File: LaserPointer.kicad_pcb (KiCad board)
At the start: 2 copper layers, 100.3 x 20.3 mm, 10 parts, among them J1 Laser Diode - 5mW 650nm Red, SW1 Mini Soft Touch Push-button S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, U1 MCP1640Bx-xCHY

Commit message: Finished
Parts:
- added H1: MountingHole_2.2mm_M2, MountingHole:MountingHole_2.2mm_M2, F.Cu at (71.1, 62.2)
- added H2: MountingHole_2.2mm_M2, MountingHole:MountingHole_2.2mm_M2, F.Cu at (156.2, 74.9)
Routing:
- net GND: vias 2 -> 4
- added copper zone on B.Cu, net GND
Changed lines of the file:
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@@
 		)
+	)
+	(footprint "MountingHole:MountingHole_2.2mm_M2"
+		(layer "F.Cu")
+		(at 156.21 74.93)
+		(descr "Mounting Hole 2.2mm, M2, no annular, generated by kicad-footprint-generator mountinghole.py")
+		(tags "mountinghole M2")
+		(property "Reference" "H2"
+			(at 0 -3.15 0)
+			(layer "F.SilkS")
+			(hide yes)
+			(effects
+				(font
+					(size 1 1)
+					(thickness 0.15)
+				)
+			)
+		)
+		(property "Value" "MountingHole_2.2mm_M2"
+			(at 0 3.15 0)
+			(layer "F.Fab")
+			(hide yes)
+			(effects
+				(font
+					(size 1 1)
+					(thickness 0.15)
+				)
+			)
+		)
+		(property "Datasheet" ""
+			(at 0 0 0)
+			(layer "F.Fab")
+			(hide yes)
+			(effects
+				(font
+					(size 1.27 1.27)
+				)
+			)
+		)
+		(property "Description" ""
+			(at 0 0 0)
+			(layer "F.Fab")
+			(hide yes)
+			(effects
+				(font
+					(size 1.27 1.27)
+				)
+			)
+		)
+		(property "KiLib_Generator" "mounting_hardware/mounting_hole"
+			(at 0 0 0)
+			(layer "F.SilkS")
+			(hide yes)
+			(effects
+				(font
+					(size 1 1)
+					(thickness 0.15)
+				)
+			)
+		)
+		(attr exclude_from_pos_files exclude_from_bom)
+		(duplicate_pad_numbers_are_jumpers no)
+		(fp_circle
+			(center 0 0)
+			(end 2.2 0)
+			(stroke
+				(width 0.15)
+				(type solid)
+			)
+			(fill no)
+			(layer "Cmts.User")
+		)
+		(fp_circle
+			(center 0 0)
+			(end 2.45 0)
+			(stroke
+				(width 0.05)
+				(type solid)
+			)
+			(fill no)
+			(layer "F.CrtYd")
+		)
+		(fp_text user "H2"
+			(at 0 0 0)
+			(layer "F.Fab")
+			(effects
+				(font
+					(size 1 1)
+					(thickness 0.15)
+				)
+			)
+		)
+		(pad "" np_thru_hole circle
+			(at 0 0)
+			(size 2.2 2.2)
+			(drill 2.2)
+			(layers "*.Cu" "*.Mask")
+		)
+		(embedded_fonts no)
 	)
 	(footprint "Capacitor_SMD:C_0805_2012Metric"
@@
 		(embedded_fonts no)
 	)
+	(footprint "MountingHole:MountingHole_2.2mm_M2"
+		(layer "F.Cu")
+		(at 71.12 62.23)
+		(descr "Mounting Hole 2.2mm, M2, no annular, generated by kicad-footprint-generator mountinghole.py")
+		(tags "mountinghole M2")
+		(property "Reference" "H1"
+			(at 0 -3.15 0)
+			(layer "F.SilkS")
+			(hide yes)
+			(effects
+				(font
+					(size 1 1)
+					(thickness 0.15)
+				)
+			)
+		)
+		(property "Value" "MountingHole_2.2mm_M2"
+			(at 0 3.15 0)
+			(layer "F.Fab")
+			(hide yes)
+			(effects
+				(font
+					(size 1 1)
+					(thickness 0.15)
+				)
+			)
+		)
+		(property "Datasheet" ""
+			(at 0 0 0)
+			(layer "F.Fab")
+			(hide yes)
+			(effects
+				(font
+					(size 1.27 1.27)
+				)
+			)
+		)
+		(property "Description" ""
+			(at 0 0 0)
+			(layer "F.Fab")
+			(hide yes)
+			(effects
+				(font
+					(size 1.27 1.27)
+				)
+			)
+		)
+		(property "KiLib_Generator" "mounting_hardware/mounting_hole"
+			(at 0 0 0)
+			(layer "F.SilkS")
+			(hide yes)
+			(effects
+				(font
+					(size 1 1)
+					(thickness 0.15)
+				)
+			)
+		)
+		(attr exclude_from_pos_files exclude_from_bom)
+		(duplicate_pad_numbers_are_jumpers no)
+		(fp_circle
+			(center 0 0)
+			(end 2.2 0)
+			(stroke
+				(width 0.15)
+				(type solid)
+			)
+			(fill no)
+			(layer "Cmts.User")
+		)
+		(fp_circle
+			(center 0 0)
+			(end 2.45 0)
+			(stroke
+				(width 0.05)
+				(type solid)
+			)
+			(fill no)
+			(layer "F.CrtYd")
+		)
+		(fp_text user "H1"
+			(at 0 0 0)
+			(layer "F.Fab")
+			(effects
+				(font
+					(size 1 1)
+					(thickness 0.15)
+				)
+			)
+		)
+		(pad "" np_thru_hole circle
+			(at 0 0)
+			(size 2.2 2.2)
+			(drill 2.2)
+			(layers "*.Cu" "*.Mask")
+		)
+		(embedded_fonts no)
+	)
 	(gr_arc
 		(start 67.31 60.42)
@@
 	)
 	(via
+		(at 135 65)
+		(size 0.6)
+		(drill 0.3)
+		(layers "F.Cu" "B.Cu")
+		(free yes)
+		(net "GND")
+	)
+	(via
 		(at 153.035 62.865)
 		(size 0.6)
@@
 		(net "GND")
 	)
+	(via
+		(at 161.036 69.088)
+		(size 0.6)
+		(drill 0.3)
+		(layers "F.Cu" "B.Cu")
+		(free yes)
+		(net "GND")
+	)
 	(segment
 		(start 151.765 66.04)
@@
 		(net "Net-(U1-SW)")
 	)
+	(zone
+		(net "GND")
+		(layer "B.Cu")
+		(name "GND_pour")
+		(hatch edge 0.5)
+		(connect_pads
+			(clearance 0.3)
+		)
+		(min_thickness 0.25)
+		(fill yes
+			(thermal_gap 0.5)
+			(thermal_bridge_width 0.5)
+			(island_removal_mode 0)
+		)
+		(polygon
+			(pts
+				(xy 60.96 55.88) (xy 60.96 81.28) (xy 172.72 81.28) (xy 172.72 55.88)
+			)
+		)
+	)
 	(embedded_fonts no)

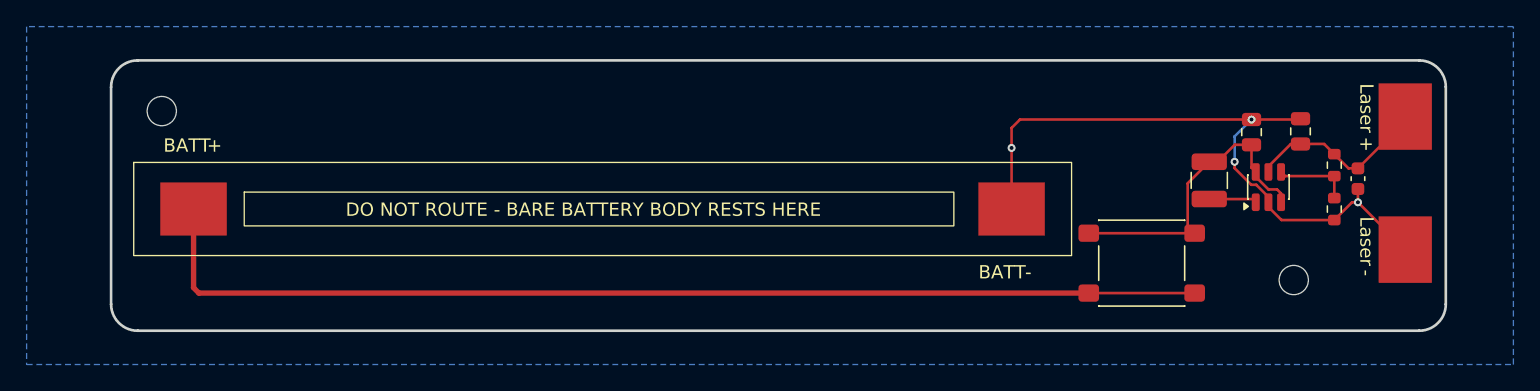
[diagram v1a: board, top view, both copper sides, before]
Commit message: Made board WAY smaller to be chcheaper, uses battery terminals now lol. Just solder leads on and use a holder
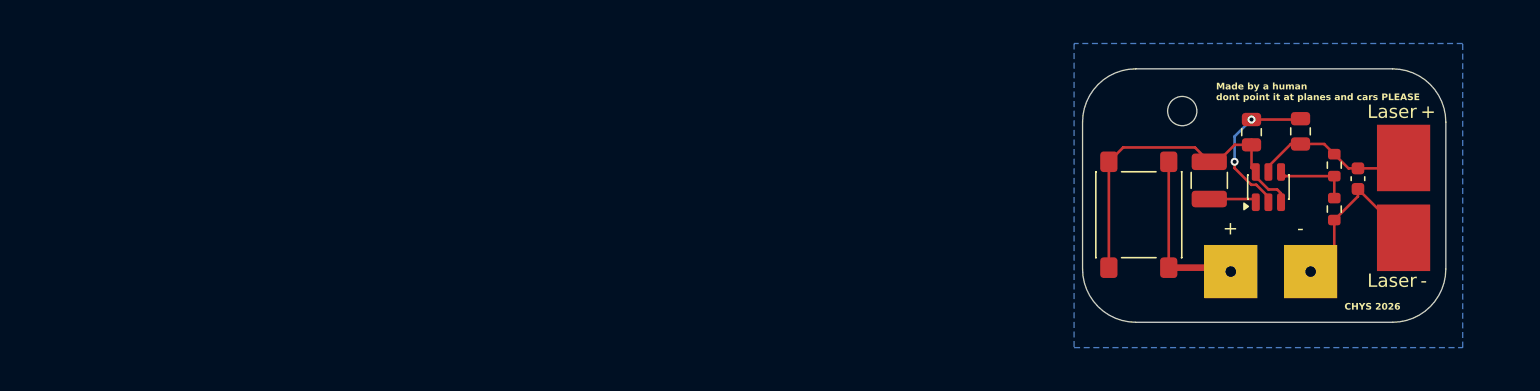
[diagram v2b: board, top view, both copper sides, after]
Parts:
- removed H1, H2: MountingHole_2.2mm_M2, MountingHole:MountingHole_2.2mm_M2
- added M2_1: MountingHole_2.2mm_M2, MountingHole:MountingHole_2.2mm_M2, F.Cu at (147.8, 62.2)
- BT1: footprint Mylibrary:BatteryHolder_Keystone_1020_1xAAA -> Mylibrary:Batt terminal pads
- moved BT1 78.1 mm to (151.5, 74.3)
- moved SW1 3.65 mm to (144.6, 70.0), turned to -90 degrees
- moved J1 1.12 mm to (164.5, 68.8)
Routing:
- net Net-(BT1-+): track 81.3 -> 12.8 mm
- net GND: track 50.2 -> 24.8 mm, vias 4 -> 2
- net Net-(U1-EN): track 23.5 -> 26.1 mm
- net Net-(J1-Pin_1): track 14.0 -> 12.4 mm
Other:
- board size 100.3 x 20.3 mm -> 27.3 x 19.1 mm
- board text added: "CHYS 2026"
- board text added: "Made by a human dont point it at planes and cars PLEASE"

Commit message: misc changes
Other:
- board text removed: "CHYS 2026"
- board text removed: "Made by a human dont point it at planes and cars PLEASE"
